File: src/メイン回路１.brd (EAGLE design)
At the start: 41 parts, among them T1 一般的なトランジスタ, T2 一般的なトランジスタ, T3 一般的なトランジスタ, T4 一般的なトランジスタ

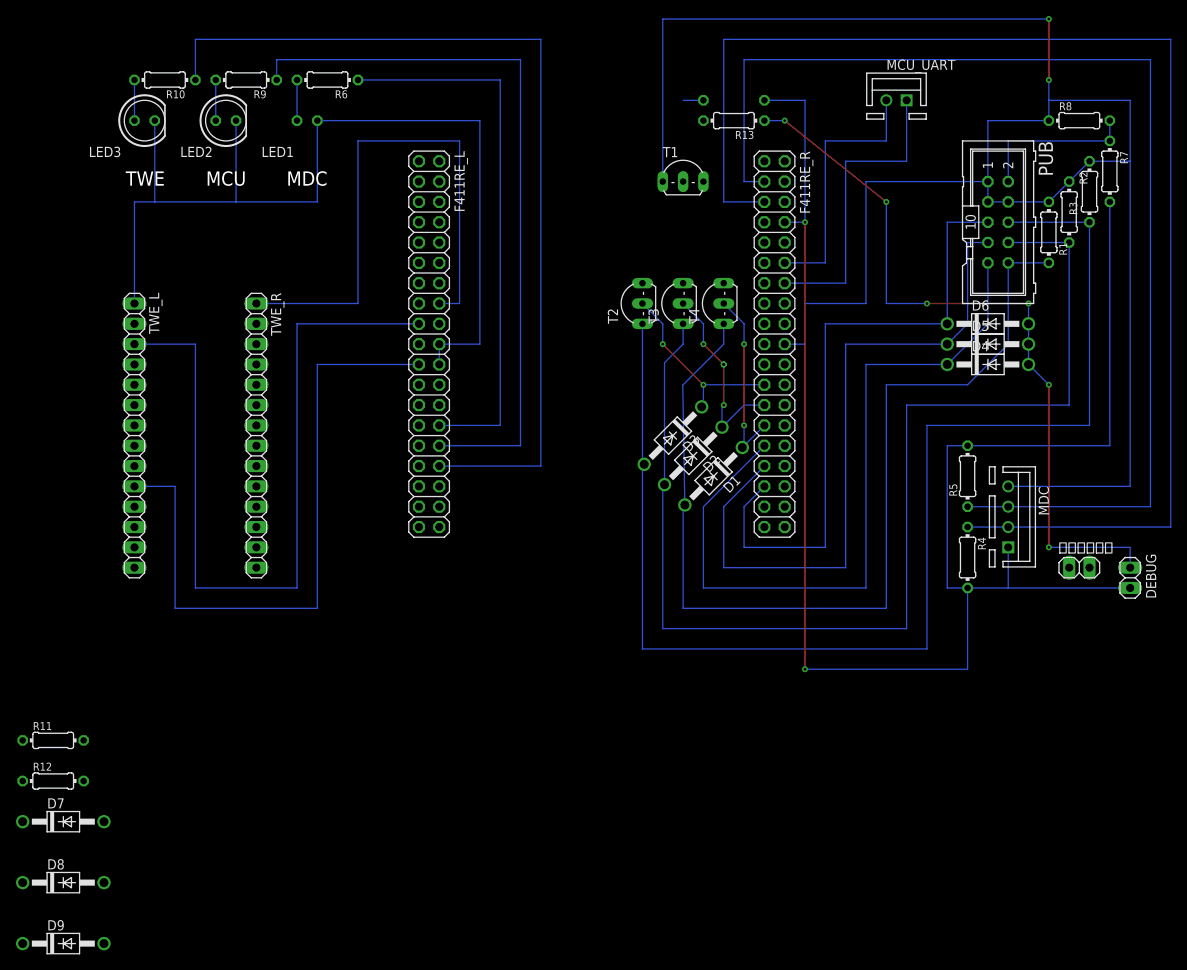
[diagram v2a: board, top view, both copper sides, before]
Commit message: 配線をDriveUnit ver2.0用に変更
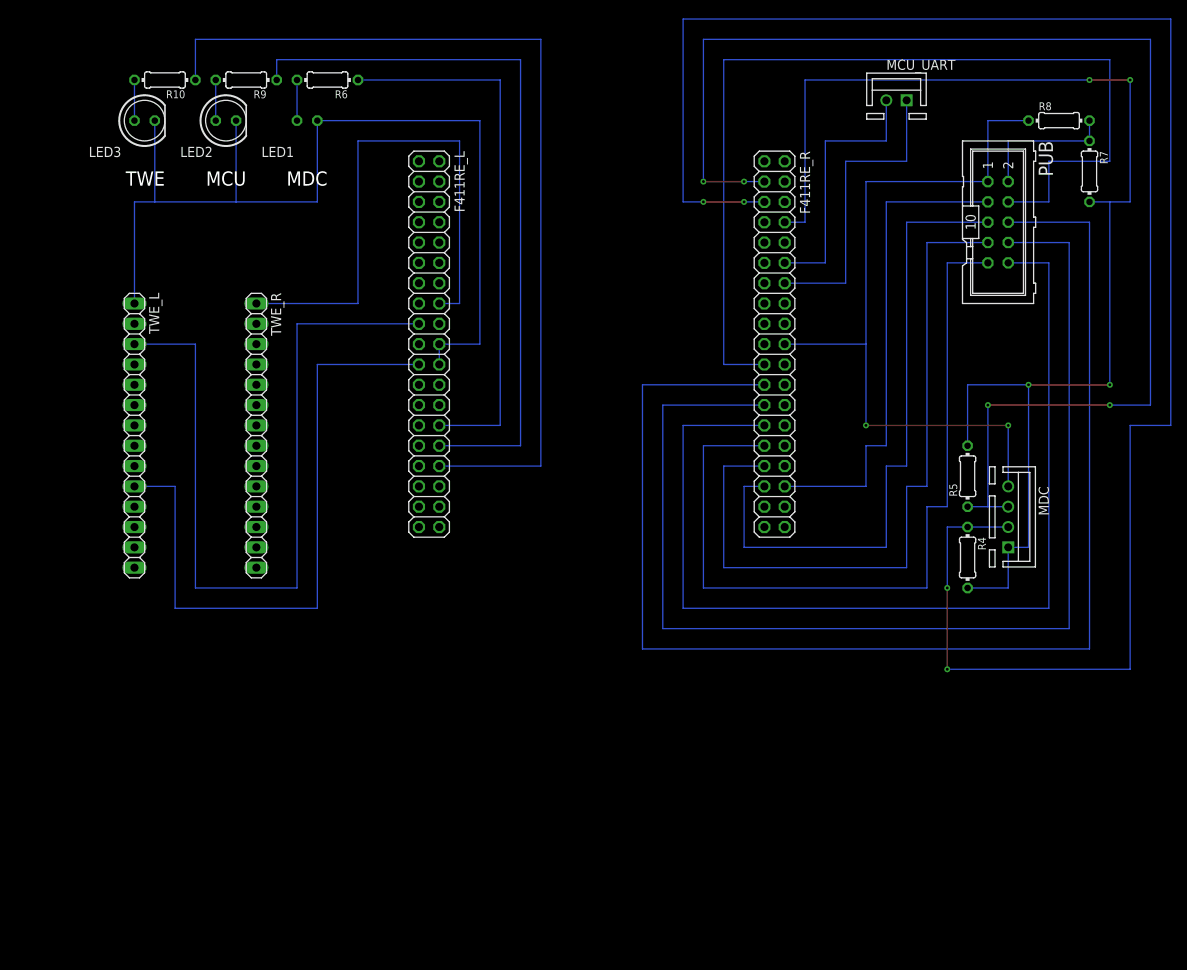
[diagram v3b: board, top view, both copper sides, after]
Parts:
- removed D1, D2, D3, D4, D5, D6, D7, D8, D9: 1N4004, diode:DO41-10
- removed DEBUG, ソケット置き: (no value), pinhead:1X02
- removed R1, R2, R3: 330, rcl:0204/7
- removed R11, R12, R13, R14: 10k, rcl:0204/7
- removed T1, T2, T3, T4: 一般的なトランジスタ, 一般的なトランジスタ:TO92-CEB
- moved R7 2.54 mm to (119.4, 52.1)
- moved R8 2.54 mm to (115.6, 58.4)
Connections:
- removed net DEBUG: D4.A, D5.A, D6.A, DEBUG.2, R13.1
- removed net N$4: R13.2, T1.B
- removed net N$5: D8.A, R11.1, T3.B
- removed net N$6: D9.A, R12.1, T2.B
- removed net N$7: D7.C, D8.C, D9.C, T1.C
- removed net N$8: D1.A, PUB.10, R1.2, T4.E
- removed net N$9: D2.A, PUB.8, R2.2, T3.E
- removed net N$Q0: D3.A, PUB.6, R3.2, T2.E
- removed net ZM: D7.A, R14.1, T4.B
- new net DIR4: F411RE_R.34, PUB.3
- new net PWM4: F411RE_R.21, PUB.4
- net DIR1: no longer D4.C
- net DIR2: no longer D5.C
- net DIR3: no longer D6.C
- net GND: no longer PUB.3, PUB.4, R1.1, R2.1, R3.1, T1.E
- net PWM1: now also PUB.10; no longer D1.C, T4.C
- net PWM2: now also PUB.8; no longer D2.C, T3.C
- net PWM3: now also PUB.6; no longer D3.C, T2.C
- net U5V: no longer DEBUG.1, R11.2, R12.2, R14.2
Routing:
- net N$Q0: track 160.3 -> 0.00 mm
- net N$9: track 146.1 -> 0.00 mm
- net GND: track 360.2 -> 215.9 mm
- net PWM3: track 23.8 -> 167.6 mm, vias 2 -> 0
- net N$8: track 123.7 -> 0.00 mm
- net PWM2: track 24.1 -> 147.3 mm, vias 4 -> 0
- net PWM4: track 0.00 -> 121.9 mm
- net PWM1: track 22.7 -> 127.0 mm, vias 2 -> 0
- net DEBUG: track 93.5 -> 0.00 mm, vias 6 -> 0
- net SDA: track 167.6 -> 228.6 mm, vias 0 -> 4
- net DIR4: track 0.00 -> 61.0 mm
- net U5V: track 205.7 -> 162.6 mm, vias 2 -> 4
- net SCL: track 147.3 -> 165.1 mm, vias 0 -> 4
- net DIR1: track 94.2 -> 101.6 mm
- net DIR2: track 87.0 -> 91.4 mm
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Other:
- board text removed: "⇐MILコネクタ付ける前に配線すること!!"
